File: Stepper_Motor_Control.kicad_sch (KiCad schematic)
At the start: 22 parts

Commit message: Stepper Motor Control Update
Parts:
- added C?: 100nF, symbol Device:C
- added IC?: AS5600-ASOT, KSZ_KiCad_Footprint_Library:SOIC127P600X175-8N, symbol KSZ_KiCad_Symbol_Library:AS5600-ASOT
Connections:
- net +3.3V: now also C?.1, IC?.1 (VDD5V), IC?.2 (VDD3V3)
- net GND: now also C?.2, IC?.4 (GND), IC?.8 (DIR)
- new net AS5600_SCL: IC?.7 (SCL)
- new net AS5600_SDA: IC?.6 (SDA)
- no-connect marks 3 -> 5
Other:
- note added: "AS5600"

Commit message: Schematic finish & ERC
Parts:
- removed R?: 1k, symbol Device:R
- added R24: 1k, symbol Device:R
- gave numbers to parts that had none: 23
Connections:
- net GND: now also C33.2
- net UART_RX: now also R24.1
- net UART_TX: now also R24.2
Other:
- note added: "VS"
- note removed: "UART"
- note removed: "VM"
- moved on the sheet: C26, C28, C30, C32, J5

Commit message: Footprint Update
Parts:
- C20, C21, C22, C23, C24, C25, C26, C27, C28, C29, C30, C32: footprint (none) -> Capacitor_SMD:C_0402_1005Metric_Pad0.74x0.62mm_HandSolder
- C31, C33: footprint (none) -> Capacitor_THT:CP_Radial_D6.3mm_P2.50mm
- J5: footprint (none) -> Connector_JST:JST_PH_S4B-PH-K_1x04_P2.00mm_Horizontal
- JP6, JP7: footprint (none) -> Jumper:SolderJumper-3_P1.3mm_Open_RoundedPad1.0x1.5mm_NumberLabels
- JP8: footprint (none) -> Jumper:SolderJumper-2_P1.3mm_Open_RoundedPad1.0x1.5mm
- R21, R24: footprint (none) -> Resistor_SMD:R_0402_1005Metric_Pad0.72x0.64mm_HandSolder
- R22, R23: footprint (none) -> Resistor_SMD:R_2010_5025Metric_Pad1.40x2.65mm_HandSolder
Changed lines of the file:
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@@
 			)
 		)
-		(property "Footprint" ""
+		(property "Footprint" "Capacitor_SMD:C_0402_1005Metric_Pad0.74x0.62mm_HandSolder"
 			(at 187.6552 38.1 0)
 			(effects
@@
 			)
 		)
-		(property "Footprint" ""
+		(property "Footprint" "Jumper:SolderJumper-3_P1.3mm_Open_RoundedPad1.0x1.5mm_NumberLabels"
 			(at 44.45 57.15 0)
 			(effects
@@
 			)
 		)
-		(property "Footprint" ""
+		(property "Footprint" "Capacitor_SMD:C_0402_1005Metric_Pad0.74x0.62mm_HandSolder"
 			(at 143.51 44.7548 0)
 			(effects
@@
 			)
 		)
-		(property "Footprint" ""
+		(property "Footprint" "Resistor_SMD:R_0402_1005Metric_Pad0.72x0.64mm_HandSolder"
 			(at 36.83 80.518 90)
 			(effects
@@
 			)
 		)
-		(property "Footprint" ""
+		(property "Footprint" "Capacitor_SMD:C_0402_1005Metric_Pad0.74x0.62mm_HandSolder"
 			(at 188.9252 67.31 0)
 			(effects
@@
 			)
 		)
-		(property "Footprint" ""
+		(property "Footprint" "Jumper:SolderJumper-2_P1.3mm_Open_RoundedPad1.0x1.5mm"
 			(at 110.49 53.34 0)
 			(effects
@@
 			)
 		)
-		(property "Footprint" ""
+		(property "Footprint" "Capacitor_THT:CP_Radial_D6.3mm_P2.50mm"
 			(at 199.0852 38.1 0)
 			(effects
@@
 			)
 		)
-		(property "Footprint" ""
+		(property "Footprint" "Capacitor_SMD:C_0402_1005Metric_Pad0.74x0.62mm_HandSolder"
 			(at 117.8052 49.53 0)
 			(effects
@@
 			)
 		)
-		(property "Footprint" ""
+		(property "Footprint" "Resistor_SMD:R_2010_5025Metric_Pad1.40x2.65mm_HandSolder"
 			(at 110.998 82.55 90)
 			(effects
@@
 			)
 		)
-		(property "Footprint" ""
+		(property "Footprint" "Capacitor_SMD:C_0402_1005Metric_Pad0.74x0.62mm_HandSolder"
 			(at 201.6252 67.31 0)
 			(effects
@@
 			)
 		)
-		(property "Footprint" ""
+		(property "Footprint" "Capacitor_SMD:C_0402_1005Metric_Pad0.74x0.62mm_HandSolder"
 			(at 176.2252 67.31 0)
 			(effects
@@
 			)
 		)
-		(property "Footprint" ""
+		(property "Footprint" "Capacitor_SMD:C_0402_1005Metric_Pad0.74x0.62mm_HandSolder"
 			(at 27.6352 151.13 0)
 			(effects
@@
 			)
 		)
-		(property "Footprint" ""
+		(property "Footprint" "Capacitor_SMD:C_0402_1005Metric_Pad0.74x0.62mm_HandSolder"
 			(at 127.9652 49.53 0)
 			(effects
@@
 			)
 		)
-		(property "Footprint" ""
+		(property "Footprint" "Capacitor_SMD:C_0402_1005Metric_Pad0.74x0.62mm_HandSolder"
 			(at 163.5252 67.31 0)
 			(effects
@@
 			)
 		)
-		(property "Footprint" ""
+		(property "Footprint" "Capacitor_SMD:C_0402_1005Metric_Pad0.74x0.62mm_HandSolder"
 			(at 176.2252 38.1 0)
 			(effects
@@
 			)
 		)
-		(property "Footprint" ""
+		(property "Footprint" "Capacitor_SMD:C_0402_1005Metric_Pad0.74x0.62mm_HandSolder"
 			(at 53.0352 78.74 0)
 			(effects
@@
 			)
 		)
-		(property "Footprint" ""
+		(property "Footprint" "Jumper:SolderJumper-3_P1.3mm_Open_RoundedPad1.0x1.5mm_NumberLabels"
 			(at 44.45 67.31 0)
 			(effects
@@
 			)
 		)
-		(property "Footprint" ""
+		(property "Footprint" "Resistor_SMD:R_0402_1005Metric_Pad0.72x0.64mm_HandSolder"
 			(at 65.278 96.52 90)
 			(effects
@@
 			)
 		)
-		(property "Footprint" ""
+		(property "Footprint" "Capacitor_SMD:C_0402_1005Metric_Pad0.74x0.62mm_HandSolder"
 			(at 163.5252 38.1 0)
 			(effects
@@
 			)
 		)
-		(property "Footprint" ""
+		(property "Footprint" "Capacitor_THT:CP_Radial_D6.3mm_P2.50mm"
 			(at 211.7852 38.1 0)
 			(effects
@@
 			)
 		)
-		(property "Footprint" ""
+		(property "Footprint" "Connector_JST:JST_PH_S4B-PH-K_1x04_P2.00mm_Horizontal"
 			(at 168.91 85.09 0)
 			(effects
@@
 			)
 		)
-		(property "Footprint" ""
+		(property "Footprint" "Resistor_SMD:R_2010_5025Metric_Pad1.40x2.65mm_HandSolder"
 			(at 111.252 80.01 90)
 			(effects

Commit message: Layout Update
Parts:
- removed C31, C33: 330uF, Capacitor_THT:CP_Radial_D6.3mm_P2.50mm, symbol Device:C_Polarized
- removed JP6, JP7: SolderJumper_3_Open, Jumper:SolderJumper-3_P1.3mm_Open_RoundedPad1.0x1.5mm_NumberLabels, symbol Jumper:SolderJumper_3_Open
- removed JP8: SolderJumper_2_Open, Jumper:SolderJumper-2_P1.3mm_Open_RoundedPad1.0x1.5mm, symbol Jumper:SolderJumper_2_Open
- added C31, C33: 10uF, Capacitor_SMD:C_0603_1608Metric_Pad1.08x0.95mm_HandSolder, symbol Device:C
- added C34: 100nF, Capacitor_SMD:C_0402_1005Metric_Pad0.74x0.62mm_HandSolder, symbol Device:C
- C27, C29: footprint Capacitor_SMD:C_0402_1005Metric_Pad0.74x0.62mm_HandSolder -> Capacitor_SMD:C_0603_1608Metric_Pad1.08x0.95mm_HandSolder
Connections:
- net +12V: now also C31.1, C33.1, C34.1
- net A1: now also J5.3 (Pin_3); no longer J5.2 (Pin_2)
- net A2: now also J5.4 (Pin_4); no longer J5.3 (Pin_3)
- net B1: now also J5.2 (Pin_2); no longer J5.1 (Pin_1)
- net B2: now also J5.1 (Pin_1); no longer J5.4 (Pin_4)
- net DIAG: now also U5.11 (DIAG)
- net GND: now also U5.10 (MS2_AD1), U5.9 (MS1_AD0), C31.2, C33.2, C34.2
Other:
- moved on the sheet: C25, C27, C29

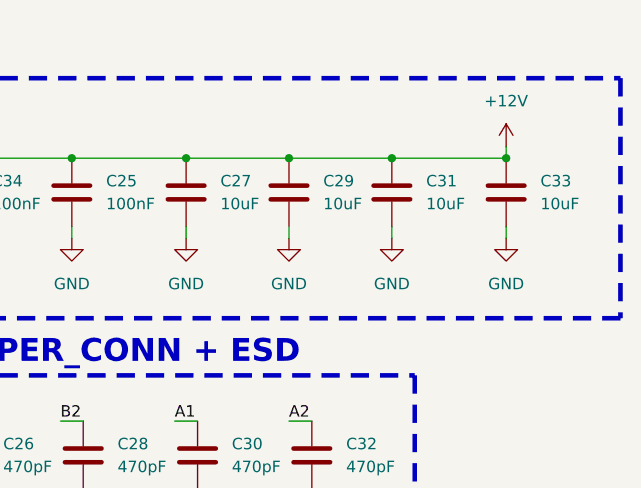
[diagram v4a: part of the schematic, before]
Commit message: Schematic check, Text adjustment & QoL changes
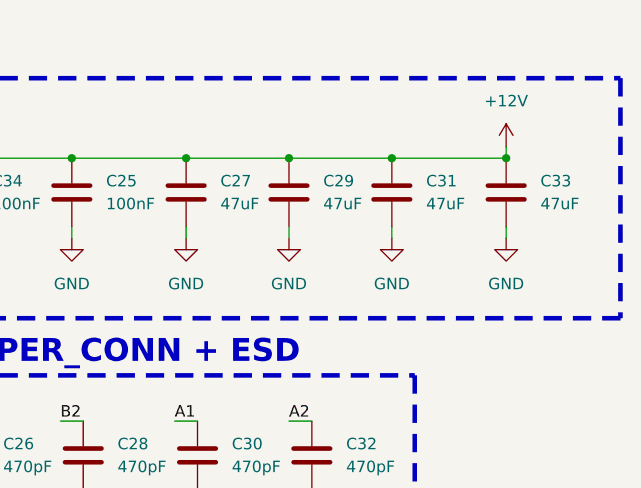
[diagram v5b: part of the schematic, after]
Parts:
- C27, C29, C31, C33: value 10uF -> 47uF
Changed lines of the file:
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@@
 			)
 		)
-		(property "Value" "10uF"
+		(property "Value" "47uF"
 			(at 201.93 35.5599 0)
 			(effects
@@
 			)
 		)
-		(property "Value" "10uF"
+		(property "Value" "47uF"
 			(at 213.36 35.5599 0)
 			(effects
@@
 			)
 		)
-		(property "Value" "10uF"
+		(property "Value" "47uF"
 			(at 226.06 35.5599 0)
 			(effects
@@
 			)
 		)
-		(property "Value" "10uF"
+		(property "Value" "47uF"
 			(at 190.5 35.5599 0)
 			(effects
